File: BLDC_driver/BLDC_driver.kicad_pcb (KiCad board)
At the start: 2 copper layers, 96 parts, among them J1 POWER, J2 CTRL, J3 JTAG, J4 USB-C 16P, Q1 AOTL66912, Q2 AOTL66912, Q3 AOTL66912, Q4 AOTL66912, Q5 AOTL66912, Q6 AOTL66912, SW1 BTN, SW2 BTN, U1 STM32F412CEUx, U2 W25Q128JVS, U3 USBLC6-2SC6, Y1 25MHz

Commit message: Layout progress
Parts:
- added R13: 500u, Marijn_KiCad:CSS2H-3920R-xxxx, F.Cu at (39.1, 111.4)
- added R14: 500u, Marijn_KiCad:CSS2H-3920R-xxxx, F.Cu at (54.1, 111.4)
- added R15: 500u, Marijn_KiCad:CSS2H-3920R-xxxx, F.Cu at (69.1, 111.4)
- J1: footprint TerminalBlock:TerminalBlock_Xinya_XY308-2.54-2P_1x02_P2.54mm_Horizontal -> Connector_AMASS:AMASS_XT60-F_1x02_P7.20mm_Vertical
- moved C10 114.8 mm to (43.6, 145.7), turned to 180 degrees
- moved C13 104.0 mm to (43.6, 115.7), turned to 180 degrees
- moved C11 100.1 mm to (58.6, 145.7), turned to 180 degrees
- moved J1 91.2 mm to (79.7, 98.8), turned to 180 degrees
- moved C14 88.7 mm to (58.6, 115.7), turned to 180 degrees
- moved C12 85.5 mm to (73.6, 145.7), turned to 180 degrees
- moved C15 73.5 mm to (73.6, 115.7), turned to 180 degrees
- moved Q4 45.4 mm to (69.7, 123.8)
- moved Q3 44.3 mm to (69.7, 153.8), turned to -90 degrees
- moved R8 41.4 mm to (95.8, 137.8)
- moved R10 41.4 mm to (95.8, 142.8)
- moved R7 41.4 mm to (95.8, 135.3)
- moved R9 41.4 mm to (95.8, 140.3)
- moved Q2 36.2 mm to (54.7, 153.8), turned to -90 degrees
- moved Q5 34.2 mm to (54.7, 123.8)
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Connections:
- net Net-(Q4-S) renamed /phase_logic/C_CSP
- net Net-(Q5-S) renamed /phase_logic/B_CSP
- net Net-(Q6-S) renamed /phase_logic/A_CSP
- J1 pad 1: +24V -> VPWR

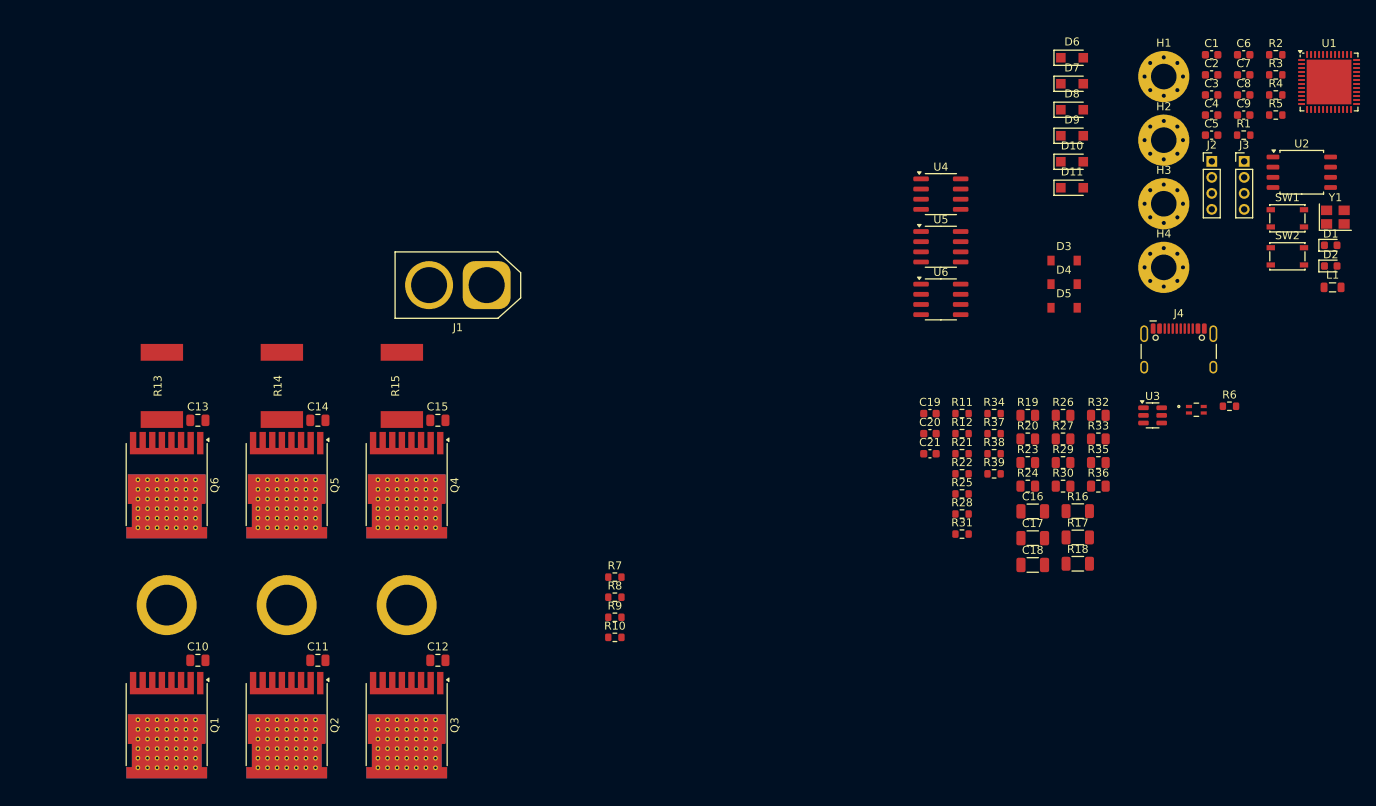
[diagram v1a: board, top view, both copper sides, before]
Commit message: Rough inverter stage layout
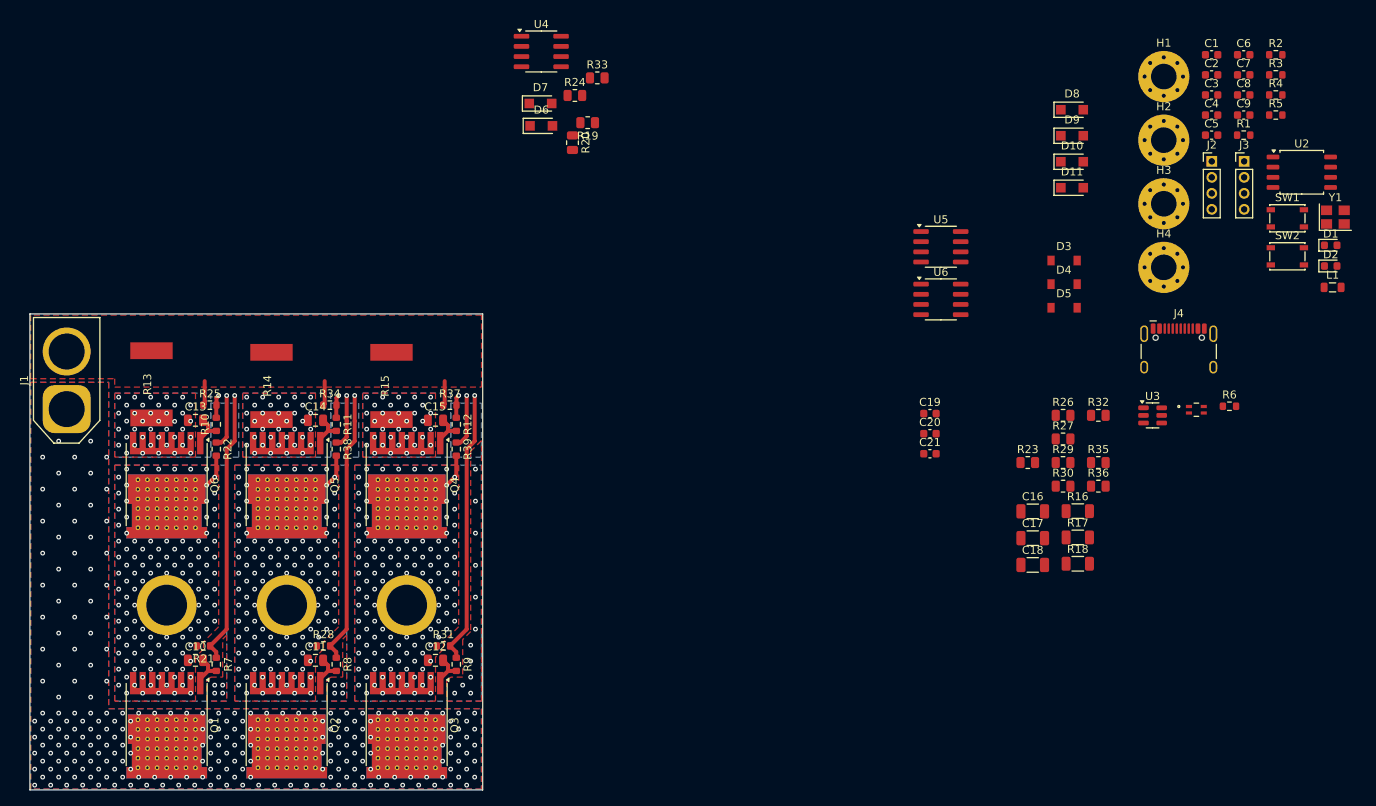
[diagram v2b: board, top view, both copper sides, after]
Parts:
- removed U1: STM32F412CEUx, Package_DFN_QFN:QFN-48-1EP_7x7mm_P0.5mm_EP5.6x5.6mm
- moved R21 97.8 mm to (44.3, 143.9)
- moved R25 94.7 mm to (45.1, 113.8)
- moved R22 93.3 mm to (45.9, 119.3), turned to -90 degrees
- moved R34 83.0 mm to (60.1, 113.8)
- moved R38 82.2 mm to (60.9, 119.3), turned to -90 degrees
- moved R28 81.5 mm to (59.3, 143.9)
- moved R11 78.2 mm to (60.9, 116.2), turned to -90 degrees
- moved R33 77.2 mm to (93.6, 72.9)
- moved R24 74.8 mm to (90.8, 75.1)
- moved R37 68.1 mm to (75.1, 113.8)
- moved R20 67.9 mm to (90.5, 81.0), turned to -90 degrees
- moved R39 67.3 mm to (75.9, 119.3), turned to -90 degrees
- moved D6 66.9 mm to (86.6, 78.9)
- moved D7 66.5 mm to (86.5, 76.1)
- moved R31 66.3 mm to (74.3, 143.9)
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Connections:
- net Net-(Q1-S) renamed /phase_logic/A
- net Net-(Q2-S) renamed /phase_logic/B
- net Net-(Q3-S) renamed /phase_logic/C
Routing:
- net Net-(D9-A): track 0.00 -> 34.4 mm, vias 0 -> 1
- net Net-(D8-A): track 0.00 -> 34.4 mm, vias 0 -> 1
- net Net-(D6-A): track 0.00 -> 34.4 mm, vias 0 -> 1
- net GND: track 0.00 -> 9.52 mm
- net /phase_logic/PHA: track 0.00 -> 6.78 mm, vias 0 -> 1
- net /phase_logic/PHB: track 0.00 -> 6.78 mm, vias 0 -> 1
- net /phase_logic/PHC: track 0.00 -> 6.72 mm, vias 0 -> 1
- net Net-(Q4-G): track 0.00 -> 4.54 mm
- net Net-(Q6-G): track 0.00 -> 4.54 mm
- net Net-(Q5-G): track 0.00 -> 4.54 mm
- net Net-(Q3-G): track 0.00 -> 4.54 mm
- net Net-(Q2-G): track 0.00 -> 4.54 mm
- net Net-(Q1-G): track 0.00 -> 4.54 mm
- net /phase_logic/C: track 0.00 -> 4.17 mm, vias 0 -> 132
- net /phase_logic/B: track 0.00 -> 4.17 mm, vias 0 -> 124
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- added copper zone on B.Cu, net /phase_logic/A
- added copper zone on F.Cu, net /phase_logic/A
- added copper zone on B.Cu, net /phase_logic/A_CSP
- added copper zone on F.Cu, net /phase_logic/A_CSP
- added copper zone on B.Cu, net /phase_logic/B
- added copper zone on F.Cu, net /phase_logic/B
- added copper zone on B.Cu, net /phase_logic/B_CSP
- added copper zone on F.Cu, net /phase_logic/B_CSP
- added copper zone on B.Cu, net /phase_logic/C
- added copper zone on F.Cu, net /phase_logic/C
- added copper zone on B.Cu, net /phase_logic/C_CSP
- added copper zone on F.Cu, net /phase_logic/C_CSP
- added copper zone on F.Cu, net GND
- added copper zone on B.Cu, net VPWR
- added copper zone on F.Cu, net VPWR
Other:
- board outline added: 56.6 x 59.5 mm
- copper layers 2 -> 4

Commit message: Layout progress
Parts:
- moved R23 106.6 mm to (43.0, 99.0)
- moved C16 101.8 mm to (52.0, 93.0), turned to -90 degrees
- moved R32 99.5 mm to (58.0, 99.0)
- moved D10 93.5 mm to (60.9, 100.0), turned to -90 degrees
- moved D8 92.6 mm to (63.2, 100.0), turned to -90 degrees
- moved C21 91.0 mm to (47.1, 96.9), turned to 180 degrees
- moved C17 89.2 mm to (67.0, 93.0), turned to -90 degrees
- moved R27 87.3 mm to (66.1, 101.0), turned to 180 degrees
- moved R26 87.1 mm to (66.1, 99.0), turned to 180 degrees
- moved D11 78.3 mm to (75.7, 99.9), turned to -90 degrees
- moved C19 75.2 mm to (62.1, 96.9), turned to 180 degrees
- moved U5 74.4 mm to (62.1, 93.4), turned to 180 degrees
- moved H2 72.7 mm to (96.1, 55.7)
- moved H1 60.2 mm to (106.5, 56.0)
- moved U6 56.8 mm to (81.2, 87.6)
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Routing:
- net /phase_logic/PHB: track 6.78 -> 32.1 mm, vias 1 -> 2
- net /phase_logic/PHA: track 6.78 -> 31.9 mm, vias 1 -> 2
- net Net-(D10-A): track 2.90 -> 18.6 mm, vias 1 -> 2
- net Net-(D7-A): track 2.90 -> 18.6 mm, vias 1 -> 2
- net Net-(D8-A): track 34.4 -> 50.0 mm, vias 1 -> 2
- net Net-(D6-A): track 34.4 -> 49.9 mm, vias 1 -> 2
- net /phase_logic/HSA: track 0.00 -> 12.0 mm
- net /phase_logic/HSB: track 0.00 -> 12.0 mm
- net GND: track 9.52 -> 17.9 mm
- net /phase_logic/LSB: track 0.00 -> 7.56 mm
- net /phase_logic/LSA: track 0.00 -> 7.50 mm
- net +12V: track 0.00 -> 5.81 mm
- net Net-(U4-HB): track 0.00 -> 2.66 mm
- net Net-(U5-HB): track 0.00 -> 2.66 mm
- net Net-(D8-K): track 0.00 -> 2.15 mm
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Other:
- board size 56.6 x 59.5 mm -> 75 x 85 mm
- board text added: "TODO: Bypass CAPS"
- board text added: "TODO: define inverter / power area"
- board text added: "TODO: middle layers in inverter stage"
- board text added: "TODO: stitching"

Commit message: Update
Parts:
- moved D9 60.0 mm to (78.2, 100.0), turned to -90 degrees
- moved R35 53.6 mm to (73.0, 99.0)
- moved R36 53.6 mm to (73.0, 101.0)
- moved R29 41.1 mm to (81.1, 99.0), turned to 180 degrees
- moved R30 41.1 mm to (81.1, 101.0), turned to 180 degrees
- moved C18 40.3 mm to (82.0, 93.0), turned to -90 degrees
- moved C20 30.4 mm to (77.1, 96.9), turned to 180 degrees
- moved U6 7.10 mm to (77.1, 93.4), turned to 180 degrees
- moved D11 0.29 mm to (75.9, 100.0)
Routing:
- net /phase_logic/PHC: track 6.72 -> 32.1 mm, vias 1 -> 2
- net Net-(D11-A): track 2.90 -> 18.5 mm, vias 1 -> 2
- net Net-(D9-A): track 34.4 -> 49.8 mm, vias 1 -> 2
- net /phase_logic/HSC: track 0.00 -> 12.0 mm
- net /phase_logic/LSC: track 0.00 -> 7.53 mm
- net GND: track 17.9 -> 22.0 mm
- net +12V: track 5.81 -> 8.68 mm
- net Net-(U6-HB): track 0.00 -> 2.66 mm
- net Net-(D11-K): track 0.00 -> 2.15 mm
- net Net-(D9-K): track 0.00 -> 2.15 mm

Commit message: New design
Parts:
- added C22: 3.3nF, Capacitor_SMD:C_0805_2012Metric, F.Cu at (209.6, 65.7)
- added C23: 3.3nF, Capacitor_SMD:C_0805_2012Metric, F.Cu at (288.3, 42.0)
- added C24: 3.3nF, Capacitor_SMD:C_0805_2012Metric, F.Cu at (288.3, 45.0)
- added C25: 3.3nF, Capacitor_SMD:C_0805_2012Metric, F.Cu at (209.6, 49.1)
- added C26: 3.3nF, Capacitor_SMD:C_0805_2012Metric, F.Cu at (238.4, 122.6)
- added C27: 3.3nF, Capacitor_SMD:C_0805_2012Metric, F.Cu at (238.4, 125.6)
- added C28: 3.3nF, Capacitor_SMD:C_0805_2012Metric, F.Cu at (209.6, 32.4)
- added C29: 3.3nF, Capacitor_SMD:C_0805_2012Metric, F.Cu at (259.7, 122.6)
- added C30: 3.3nF, Capacitor_SMD:C_0805_2012Metric, F.Cu at (259.7, 125.6)
- added C31: 3.3nF, Capacitor_SMD:C_0805_2012Metric, F.Cu at (192.7, 49.1)
- added C32: 3.3nF, Capacitor_SMD:C_0805_2012Metric, F.Cu at (217.1, 122.6)
- added C33: 3.3nF, Capacitor_SMD:C_0805_2012Metric, F.Cu at (217.1, 125.6)
- added C34: 3.3nF, Capacitor_SMD:C_0805_2012Metric, F.Cu at (192.7, 32.4)
- added C35: 3.3nF, Capacitor_SMD:C_0805_2012Metric, F.Cu at (281.0, 122.6)
- added C36: 3.3nF, Capacitor_SMD:C_0805_2012Metric, F.Cu at (281.0, 125.6)
- added C37: 3.3nF, Capacitor_SMD:C_0805_2012Metric, F.Cu at (192.7, 65.7)
- added HS1: SK_92/50_SA, Marijn_KiCad:SK_92-50_SA, B.Cu at (112.0, 112.0)
- added Q10: AOTL66912, Package_TO_SOT_SMD:Infineon_PG-HSOF-8-1_ThermalVias, F.Cu at (130.0, 101.3)
- added Q11: AOTL66912, Package_TO_SOT_SMD:Infineon_PG-HSOF-8-1_ThermalVias, F.Cu at (130.0, 112.0)
- added Q12: AOTL66912, Package_TO_SOT_SMD:Infineon_PG-HSOF-8-1_ThermalVias, F.Cu at (130.0, 122.7)
- added Q13: AOTL66912, Package_TO_SOT_SMD:Infineon_PG-HSOF-8-1_ThermalVias, F.Cu at (94.0, 134.6)
- added Q14: AOTL66912, Package_TO_SOT_SMD:Infineon_PG-HSOF-8-1_ThermalVias, F.Cu at (94.0, 145.3)
- added Q15: AOTL66912, Package_TO_SOT_SMD:Infineon_PG-HSOF-8-1_ThermalVias, F.Cu at (94.0, 156.0)
- added Q16: AOTL66912, Package_TO_SOT_SMD:Infineon_PG-HSOF-8-1_ThermalVias, F.Cu at (130.0, 134.6)
- added Q17: AOTL66912, Package_TO_SOT_SMD:Infineon_PG-HSOF-8-1_ThermalVias, F.Cu at (130.0, 145.3)
- added Q18: AOTL66912, Package_TO_SOT_SMD:Infineon_PG-HSOF-8-1_ThermalVias, F.Cu at (130.0, 156.0)
- added Q7: AOTL66912, Package_TO_SOT_SMD:Infineon_PG-HSOF-8-1_ThermalVias, F.Cu at (94.0, 101.3)
- added Q8: AOTL66912, Package_TO_SOT_SMD:Infineon_PG-HSOF-8-1_ThermalVias, F.Cu at (94.0, 112.0)
- added Q9: AOTL66912, Package_TO_SOT_SMD:Infineon_PG-HSOF-8-1_ThermalVias, F.Cu at (94.0, 122.7)
- added R40: 2R2, Resistor_SMD:R_0603_1608Metric, F.Cu at (238.2, 128.3)
- added R41: 2R2, Resistor_SMD:R_0603_1608Metric, F.Cu at (238.2, 130.9)
- added R42: 2R2, Resistor_SMD:R_0603_1608Metric, F.Cu at (213.8, 32.1)
- added R43: 2R2, Resistor_SMD:R_0603_1608Metric, F.Cu at (259.5, 128.3)
- added R44: 2R2, Resistor_SMD:R_0603_1608Metric, F.Cu at (259.5, 130.9)
- added R45: 2R2, Resistor_SMD:R_0603_1608Metric, F.Cu at (196.9, 48.8)
- added R46: 2R2, Resistor_SMD:R_0603_1608Metric, F.Cu at (216.9, 128.3)
- added R47: 2R2, Resistor_SMD:R_0603_1608Metric, F.Cu at (216.9, 130.9)
- added R48: 2R2, Resistor_SMD:R_0603_1608Metric, F.Cu at (196.9, 32.1)
- added R49: 2R2, Resistor_SMD:R_0603_1608Metric, F.Cu at (280.8, 128.3)
- added R50: 2R2, Resistor_SMD:R_0603_1608Metric, F.Cu at (280.8, 130.9)
- added R51: 2R2, Resistor_SMD:R_0603_1608Metric, F.Cu at (196.9, 65.5)
- added U1: STM32F412CEUx, Package_DFN_QFN:QFN-48-1EP_7x7mm_P0.5mm_EP5.6x5.6mm, F.Cu at (187.6, 136.2)
- C1, C2, C3, C4: value 100n -> 820u/100v; footprint Capacitor_SMD:C_0603_1608Metric -> Capacitor_THT:C_Radial_D18.0mm_H35.5mm_P7.50mm; moved to B.Cu
- C10, C11, C14: value 3.3nF -> 100n; footprint Capacitor_SMD:C_0805_2012Metric -> Capacitor_SMD:C_0603_1608Metric
- C12, C13: value 3.3nF -> 12p; footprint Capacitor_SMD:C_0805_2012Metric -> Capacitor_SMD:C_0603_1608Metric
- C15: value 3.3nF -> 4u7/25V; footprint Capacitor_SMD:C_0805_2012Metric -> Capacitor_SMD:C_1206_3216Metric
- C16, C18: value 4u7/25V -> 100n; footprint Capacitor_SMD:C_1206_3216Metric -> Capacitor_SMD:C_0603_1608Metric
- C19: value 100n -> 4u7/25V; footprint Capacitor_SMD:C_0603_1608Metric -> Capacitor_SMD:C_1206_3216Metric
- C20, C21: value 100n -> 3.3nF; footprint Capacitor_SMD:C_0603_1608Metric -> Capacitor_SMD:C_0805_2012Metric
- C5: value 4u7 -> 100n
- C8: value 12p -> 100n
- C9: value 12p -> 4u7
- D10, D11, D9: value PMEG6010ER,115 -> SL110PL; footprint Diode_SMD:Nexperia_CFP3_SOD-123W -> Marijn_KiCad:SOD-123FL
- D3, D4, D5: value SL110PL -> PMEG6010ER,115; footprint Marijn_KiCad:SOD-123FL -> Diode_SMD:Nexperia_CFP3_SOD-123W
- J1: value POWER -> CTRL; footprint Connector_AMASS:AMASS_XT60-F_1x02_P7.20mm_Vertical -> Connector_PinHeader_2.00mm:PinHeader_1x04_P2.00mm_Vertical
- J2: value CTRL -> POWER; footprint Connector_PinHeader_2.00mm:PinHeader_1x04_P2.00mm_Vertical -> Connector_AMASS:AMASS_XT60-F_1x02_P7.20mm_Vertical
- R10, R11, R12, R22, R7, R8, R9: value 2R2 -> 10R; footprint Resistor_SMD:R_0603_1608Metric -> Resistor_SMD:R_0805_2012Metric
- R13, R14, R15: value 500u -> 47R; footprint Marijn_KiCad:CSS2H-3920R-xxxx -> Resistor_SMD:R_0603_1608Metric
- R16, R17, R18: value 33k -> 2R2; footprint Resistor_SMD:R_1206_3216Metric -> Resistor_SMD:R_0603_1608Metric
- R21: value 47R -> 10R; footprint Resistor_SMD:R_0603_1608Metric -> Resistor_SMD:R_0805_2012Metric
- R25: value 47R -> 200u; footprint Resistor_SMD:R_0603_1608Metric -> Marijn_KiCad:CSS2H-3920R-xxxx
- R26, R27: value 10R -> 200u; footprint Resistor_SMD:R_0805_2012Metric -> Marijn_KiCad:CSS2H-3920R-xxxx
- R29, R30: value 10R -> 47R; footprint Resistor_SMD:R_0805_2012Metric -> Resistor_SMD:R_0603_1608Metric
- R31: value 47R -> 33k; footprint Resistor_SMD:R_0603_1608Metric -> Resistor_SMD:R_1206_3216Metric
- R32, R33: value 10R -> 33k; footprint Resistor_SMD:R_0805_2012Metric -> Resistor_SMD:R_1206_3216Metric
- R34, R37: value 47R -> 2R2
- R35, R36: value 10R -> 2R2; footprint Resistor_SMD:R_0805_2012Metric -> Resistor_SMD:R_0603_1608Metric
- moved C21 242.7 mm to (288.3, 70.3), turned to 0 degrees
- moved R38 237.4 mm to (288.1, 50.2), turned to 0 degrees
- moved R34 231.6 mm to (288.1, 73.1)
- moved R37 223.0 mm to (288.1, 47.7)
- moved R35 216.3 mm to (288.1, 75.6)
- moved C20 213.3 mm to (288.3, 67.3), turned to 0 degrees
- moved R21 176.6 mm to (213.4, 93.0)
- moved R24 170.4 mm to (213.4, 101.8)
- moved R23 170.4 mm to (213.4, 98.9)
- moved R22 169.1 mm to (213.4, 95.9), turned to 0 degrees
- moved R7 167.4 mm to (204.6, 93.0), turned to 0 degrees
- moved R13 166.6 mm to (204.4, 112.1), turned to 0 degrees
- moved J1 163.1 mm to (190.2, 121.0), turned to 0 degrees
- moved D10 163.1 mm to (224.0, 95.9), turned to 0 degrees
- moved R33 160.6 mm to (218.4, 109.8)
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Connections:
- net /phase_logic/A_HI renamed /inverter stage/A_HI
- net /phase_logic/A_LI renamed /inverter stage/A_LI
- net /phase_logic/B_HI renamed /inverter stage/B_HI
- net /phase_logic/B_LI renamed /inverter stage/B_LI
- net /phase_logic/C_HI renamed /inverter stage/C_HI
- net /phase_logic/C_LI renamed /inverter stage/C_LI
- C1 pad 1: +3V3 -> VPWR
- C10 pad 1: Net-(Q1-G) -> +3.3VA
- C10 pad 2: /phase_logic/A -> GND
- C11 pad 1: Net-(Q2-G) -> GND
- C11 pad 2: /phase_logic/B -> /NRST
- C12 pad 1: Net-(Q3-G) -> /HSE_IN
- C12 pad 2: /phase_logic/C -> GND
- C13 pad 1: Net-(Q6-G) -> Net-(C13-Pad1)
- C13 pad 2: /phase_logic/A_CSP -> GND
- C14 pad 1: Net-(Q5-G) -> +12V
- C14 pad 2: /phase_logic/B_CSP -> GND
- C15 pad 1: Net-(Q4-G) -> /inverter stage/PHA
- C15 pad 2: /phase_logic/C_CSP -> Net-(U4-HB)
- C16 pad 1: /phase_logic/PHA -> +12V
- C16 pad 2: Net-(U4-HB) -> GND
- C17 pad 1: /phase_logic/PHB -> /inverter stage/PHB
- C18 pad 1: /phase_logic/PHC -> +12V
- C18 pad 2: Net-(U6-HB) -> GND
- C19 pad 1: +12V -> /inverter stage/PHC
- C19 pad 2: GND -> Net-(U6-HB)
- C2 pad 1: +3V3 -> VPWR
- C20 pad 1: +12V -> Net-(Q1-G)
- C20 pad 2: GND -> /inverter stage/A
- C21 pad 1: +12V -> Net-(Q2-G)
- C21 pad 2: GND -> /inverter stage/A
- C3 pad 1: +3V3 -> VPWR
- C4 pad 1: +3V3 -> VPWR
- C6 pad 1: +3.3VA -> +3V3
- C7 pad 1: GND -> +3V3
- C7 pad 2: /NRST -> GND
- C8 pad 1: /HSE_IN -> +3V3
- C9 pad 1: Net-(C9-Pad1) -> +3V3
- D10 pad 1: Net-(D10-K) -> /inverter stage/PHB
- D10 pad 2: Net-(D10-A) -> GND
- D11 pad 1: Net-(D11-K) -> /inverter stage/PHC
- D11 pad 2: Net-(D11-A) -> GND
- D3 pad 1: /phase_logic/PHA -> Net-(D3-K)
- D3 pad 2: GND -> /inverter stage/HA
- D4 pad 1: /phase_logic/PHB -> Net-(D4-K)
- D4 pad 2: GND -> /inverter stage/HB
- D5 pad 1: /phase_logic/PHC -> Net-(D5-K)
- D5 pad 2: GND -> /inverter stage/HC
- D6 pad 2: Net-(D6-A) -> /inverter stage/LA
- D7 pad 2: Net-(D7-A) -> /inverter stage/LB
- D8 pad 2: Net-(D8-A) -> /inverter stage/LC
- D9 pad 1: Net-(D9-K) -> /inverter stage/PHA
- D9 pad 2: Net-(D9-A) -> GND
- J1 pad 1: VPWR -> /CTRL_SPI_MOSI
- J1 pad 2: GND -> /CTRL_SPI_MISO
- J2 pad 1: /CTRL_SPI_MOSI -> VPWR
- J2 pad 2: /CTRL_SPI_MISO -> GND
- J5 pad 1: /phase_logic/A -> /inverter stage/A
- J6 pad 1: /phase_logic/B -> /inverter stage/B
- J7 pad 1: /phase_logic/C -> /inverter stage/C
- Q1 pad 2: /phase_logic/A -> /inverter stage/A
- Q2 pad 2: /phase_logic/B -> /inverter stage/A
- Q3 pad 2: /phase_logic/C -> /inverter stage/A
- Q4 pad 2: /phase_logic/C_CSP -> /inverter stage/A_CSP
- Q4 pad 3: /phase_logic/C -> /inverter stage/A
- Q5 pad 2: /phase_logic/B_CSP -> /inverter stage/A_CSP
- Q5 pad 3: /phase_logic/B -> /inverter stage/A
- Q6 pad 2: /phase_logic/A_CSP -> /inverter stage/A_CSP
- Q6 pad 3: /phase_logic/A -> /inverter stage/A
- R10 pad 1: Net-(D7-A) -> /inverter stage/HSA
- R10 pad 2: Net-(Q6-G) -> /inverter stage/HA
- R11 pad 1: Net-(D10-A) -> /inverter stage/HSB
- R11 pad 2: Net-(Q5-G) -> /inverter stage/HB
- R12 pad 1: Net-(D11-A) -> /inverter stage/HSC
- R12 pad 2: Net-(Q4-G) -> /inverter stage/HC
- R13 pad 1: /phase_logic/A_CSP -> /inverter stage/A
- R13 pad 2: GND -> /inverter stage/HA
- R14 pad 1: /phase_logic/B_CSP -> /inverter stage/B
- R14 pad 2: GND -> /inverter stage/HB
- R15 pad 1: /phase_logic/C_CSP -> /inverter stage/C
- R15 pad 2: GND -> /inverter stage/HC
- R16 pad 1: GND -> /inverter stage/PHA
- R16 pad 2: /phase_logic/PHA -> /inverter stage/A
- R17 pad 1: GND -> /inverter stage/PHB
- R17 pad 2: /phase_logic/PHB -> /inverter stage/B
- R18 pad 1: GND -> /inverter stage/PHC
- R18 pad 2: /phase_logic/PHC -> /inverter stage/C
- R19 pad 1: /phase_logic/HSA -> /inverter stage/LSA
- R20 pad 1: /phase_logic/HSA -> /inverter stage/LSB
- R20 pad 2: Net-(D6-A) -> Net-(D7-K)
- R21 pad 1: /phase_logic/A -> /inverter stage/LSC
- R21 pad 2: Net-(D6-A) -> Net-(D8-K)
- R22 pad 1: /phase_logic/PHA -> /inverter stage/LSA
- R22 pad 2: /phase_logic/A -> /inverter stage/LA
- R23 pad 1: /phase_logic/LSA -> /inverter stage/LSB
- R23 pad 2: Net-(D7-K) -> /inverter stage/LB
- R24 pad 1: /phase_logic/LSA -> /inverter stage/LSC
- R24 pad 2: Net-(D7-A) -> /inverter stage/LC
- R25 pad 1: GND -> /inverter stage/A_CSP
- R25 pad 2: Net-(D7-A) -> GND
- R26 pad 1: /phase_logic/HSB -> /inverter stage/B_CSP
- R26 pad 2: Net-(D8-K) -> GND
- R27 pad 1: /phase_logic/HSB -> /inverter stage/C_CSP
- R27 pad 2: Net-(D8-A) -> GND
- R28 pad 1: /phase_logic/B -> GND
- R28 pad 2: Net-(D8-A) -> /inverter stage/LA
- R29 pad 1: /phase_logic/HSC -> GND
- R29 pad 2: Net-(D9-K) -> /inverter stage/LB
- R30 pad 1: /phase_logic/HSC -> GND
- R30 pad 2: Net-(D9-A) -> /inverter stage/LC
- R31 pad 1: /phase_logic/C -> GND
- R31 pad 2: Net-(D9-A) -> /inverter stage/PHA
- R32 pad 1: /phase_logic/LSB -> GND
- R32 pad 2: Net-(D10-K) -> /inverter stage/PHB
- R33 pad 1: /phase_logic/LSB -> GND
- R33 pad 2: Net-(D10-A) -> /inverter stage/PHC
- R34 pad 1: GND -> /inverter stage/HA
- R34 pad 2: Net-(D10-A) -> Net-(Q1-G)
- R35 pad 1: /phase_logic/LSC -> /inverter stage/HA
- R35 pad 2: Net-(D11-K) -> Net-(Q2-G)
- R36 pad 1: /phase_logic/LSC -> /inverter stage/HA
- R36 pad 2: Net-(D11-A) -> Net-(Q3-G)
- R37 pad 1: GND -> /inverter stage/LA
- R37 pad 2: Net-(D11-A) -> Net-(Q4-G)
- R38 pad 1: /phase_logic/PHB -> /inverter stage/LA
- R38 pad 2: /phase_logic/B -> Net-(Q5-G)
- R39 pad 1: /phase_logic/PHC -> /inverter stage/LA
- R39 pad 2: /phase_logic/C -> Net-(Q6-G)
- R4 pad 2: Net-(C9-Pad1) -> Net-(C13-Pad1)
- R7 pad 1: Net-(D6-A) -> /inverter stage/HSA
- R7 pad 2: Net-(Q1-G) -> Net-(D3-K)
- R8 pad 1: Net-(D8-A) -> /inverter stage/HSB
- R8 pad 2: Net-(Q2-G) -> Net-(D4-K)
- R9 pad 1: Net-(D9-A) -> /inverter stage/HSC
- R9 pad 2: Net-(Q3-G) -> Net-(D5-K)
- U4 pad 3: /phase_logic/HSA -> /inverter stage/HSA
- U4 pad 4: /phase_logic/PHA -> /inverter stage/PHA
- U4 pad 8: /phase_logic/LSA -> /inverter stage/LSA
- U5 pad 3: /phase_logic/HSB -> /inverter stage/HSB
- U5 pad 4: /phase_logic/PHB -> /inverter stage/PHB
- U5 pad 8: /phase_logic/LSB -> /inverter stage/LSB
- U6 pad 3: /phase_logic/HSC -> /inverter stage/HSC
- U6 pad 4: /phase_logic/PHC -> /inverter stage/PHC
- U6 pad 8: /phase_logic/LSC -> /inverter stage/LSC
- Y1 pad 3: Net-(C9-Pad1) -> Net-(C13-Pad1)
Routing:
- net Net-(D8-A): track 50.0 -> 0.00 mm, vias 2 -> 0
- net Net-(D6-A): track 49.9 -> 0.00 mm, vias 2 -> 0
- net Net-(D9-A): track 49.8 -> 0.00 mm, vias 2 -> 0
- net /phase_logic/PHB: track 32.1 -> 0.00 mm, vias 2 -> 0
- net /phase_logic/PHC: track 32.1 -> 0.00 mm, vias 2 -> 0
- net /phase_logic/PHA: track 31.9 -> 0.00 mm, vias 2 -> 0
- net GND: track 22.0 -> 0.00 mm
- net Net-(D10-A): track 18.6 -> 0.00 mm, vias 2 -> 0
- net Net-(D7-A): track 18.6 -> 0.00 mm, vias 2 -> 0
- net Net-(D11-A): track 18.5 -> 0.00 mm, vias 2 -> 0
- net /phase_logic/HSA: track 12.0 -> 0.00 mm
- net /phase_logic/HSC: track 12.0 -> 0.00 mm
- net /phase_logic/HSB: track 12.0 -> 0.00 mm
- net +12V: track 8.68 -> 0.00 mm
- net /phase_logic/LSB: track 7.56 -> 0.00 mm
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- added copper zone on B.Cu, net /inverter stage/A
- added copper zone on F.Cu, net /inverter stage/A
- added copper zone on B.Cu, net /inverter stage/A_CSP
- added copper zone on F.Cu, net /inverter stage/A_CSP
- added copper zone on B.Cu, net /inverter stage/B
- added copper zone on F.Cu, net /inverter stage/B
- added copper zone on B.Cu, net /inverter stage/B_CSP
- added copper zone on F.Cu, net /inverter stage/B_CSP
- added copper zone on B.Cu, net /inverter stage/C
- added copper zone on F.Cu, net /inverter stage/C
- added copper zone on B.Cu, net /inverter stage/C_CSP
- added copper zone on F.Cu, net /inverter stage/C_CSP
- added copper zone on B.Cu, net GND
- added copper zone on In1.Cu, net GND
- added copper zone on In2.Cu, net GND
- added copper zone on In1.Cu, net VPWR
- removed copper zone on B.Cu, net /phase_logic/A
- removed copper zone on F.Cu, net /phase_logic/A
- removed copper zone on B.Cu, net /phase_logic/A_CSP
- removed copper zone on F.Cu, net /phase_logic/A_CSP
- removed copper zone on B.Cu, net /phase_logic/B
- removed copper zone on F.Cu, net /phase_logic/B
- removed copper zone on B.Cu, net /phase_logic/B_CSP
- removed copper zone on F.Cu, net /phase_logic/B_CSP
- removed copper zone on B.Cu, net /phase_logic/C
- removed copper zone on F.Cu, net /phase_logic/C
- removed copper zone on B.Cu, net /phase_logic/C_CSP
- removed copper zone on F.Cu, net /phase_logic/C_CSP
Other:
- board size 75 x 85 mm -> 100 x 100 mm
- board text removed: "TODO: Bypass CAPS"
- board text removed: "TODO: define inverter / power area"
- board text removed: "TODO: middle layers in inverter stage"
- board text removed: "TODO: stitching"

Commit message: Layout progress
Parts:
- removed the R34 at (288.1, 73.1)
- removed the R35 at (288.1, 75.6)
- removed the R36 at (213.8, 65.5)
- removed R37, R38, R39, R40, R41, R42, R43, R44, R45, R46, R47, R48, R49, R50, R51: 2R2, Resistor_SMD:R_0603_1608Metric
- added R26: 500u, Marijn_KiCad:CSS2H-3920R-xxxx, F.Cu at (142.9, 68.0)
- added R28: 500u, Marijn_KiCad:CSS2H-3920R-xxxx, F.Cu at (142.9, 122.7)
- added R30: 500u, Marijn_KiCad:CSS2H-3920R-xxxx, F.Cu at (142.9, 156.0)
- R25: value 200u -> 500u
- R27: renamed from R26; value 200u -> 500u
- R29: renamed from R27; value 200u -> 500u
- moved C21 186.1 mm to (102.7, 82.9)
- moved C20 185.7 mm to (102.7, 72.2)
- moved C34 156.4 mm to (102.7, 160.2)
- moved C24 153.4 mm to (139.7, 82.9), turned to 180 degrees
- moved C23 151.6 mm to (139.7, 72.2), turned to 180 degrees
- moved C36 143.3 mm to (139.7, 149.5), turned to 180 degrees
- moved C28 142.7 mm to (102.7, 126.9)
- moved C35 142.2 mm to (139.7, 138.8), turned to 180 degrees
- moved C26 136.8 mm to (102.7, 105.5)
- moved C27 136.0 mm to (102.7, 116.2)
- moved C29 121.2 mm to (139.7, 105.5), turned to 180 degrees
- moved C30 120.3 mm to (139.7, 116.2), turned to 180 degrees
- moved C33 116.9 mm to (102.7, 149.5)
- moved C32 115.6 mm to (102.7, 138.8)
- moved C22 110.4 mm to (102.7, 93.6)
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- renumbered R28 to R31, R29 to R32, R30 to R33, R31 to R34, R32 to R35, R33 to R36
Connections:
- C20 pad 1: Net-(Q1-G) -> /inverter stage/HA
- C21 pad 1: Net-(Q2-G) -> /inverter stage/HA
- C22 pad 1: Net-(Q3-G) -> /inverter stage/HA
- C23 pad 1: Net-(Q4-G) -> /inverter stage/LA
- C24 pad 1: Net-(Q5-G) -> /inverter stage/LA
- C25 pad 1: Net-(Q6-G) -> /inverter stage/LA
- C26 pad 1: Net-(Q7-G) -> /inverter stage/HB
- C27 pad 1: Net-(Q8-G) -> /inverter stage/HB
- C28 pad 1: Net-(Q9-G) -> /inverter stage/HB
- C29 pad 1: Net-(Q10-G) -> /inverter stage/LB
- C30 pad 1: Net-(Q11-G) -> /inverter stage/LB
- C31 pad 1: Net-(Q12-G) -> /inverter stage/LB
- C32 pad 1: Net-(Q13-G) -> /inverter stage/HC
- C33 pad 1: Net-(Q14-G) -> /inverter stage/HC
- C34 pad 1: Net-(Q15-G) -> /inverter stage/HC
- C35 pad 1: Net-(Q16-G) -> /inverter stage/LC
- C36 pad 1: Net-(Q17-G) -> /inverter stage/LC
- C37 pad 1: Net-(Q18-G) -> /inverter stage/LC
- Q1 pad 1: Net-(Q1-G) -> /inverter stage/HA
- Q10 pad 1: Net-(Q10-G) -> /inverter stage/LB
- Q11 pad 1: Net-(Q11-G) -> /inverter stage/LB
- Q12 pad 1: Net-(Q12-G) -> /inverter stage/LB
- Q13 pad 1: Net-(Q13-G) -> /inverter stage/HC
- Q14 pad 1: Net-(Q14-G) -> /inverter stage/HC
- Q15 pad 1: Net-(Q15-G) -> /inverter stage/HC
- Q16 pad 1: Net-(Q16-G) -> /inverter stage/LC
- Q17 pad 1: Net-(Q17-G) -> /inverter stage/LC
- Q18 pad 1: Net-(Q18-G) -> /inverter stage/LC
- Q2 pad 1: Net-(Q2-G) -> /inverter stage/HA
- Q3 pad 1: Net-(Q3-G) -> /inverter stage/HA
- Q4 pad 1: Net-(Q4-G) -> /inverter stage/LA
- Q5 pad 1: Net-(Q5-G) -> /inverter stage/LA
- Q6 pad 1: Net-(Q6-G) -> /inverter stage/LA
- Q7 pad 1: Net-(Q7-G) -> /inverter stage/HB
- Q8 pad 1: Net-(Q8-G) -> /inverter stage/HB
- Q9 pad 1: Net-(Q9-G) -> /inverter stage/HB
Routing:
- net /inverter stage/HC: track 0.00 -> 104.8 mm
- net /inverter stage/HA: track 0.00 -> 98.6 mm
- net /inverter stage/HB: track 0.00 -> 89.0 mm, vias 0 -> 2
- net /inverter stage/LB: track 0.00 -> 43.6 mm, vias 0 -> 6
- net /inverter stage/LC: track 0.00 -> 43.5 mm, vias 0 -> 6
- net /inverter stage/LA: track 0.00 -> 42.6 mm, vias 0 -> 6
- net /inverter stage/B: track 0.00 -> 23.7 mm, vias 0 -> 2
- net /inverter stage/PHB: track 0.00 -> 11.1 mm
- net Net-(U5-HB): track 0.00 -> 2.69 mm
- net GND: track 0.00 -> 2.22 mm
- net /inverter stage/HSA: track 0.00 -> 2.11 mm
- net /inverter stage/LSC: track 0.00 -> 2.11 mm
- net /inverter stage/HSB: track 0.00 -> 2.11 mm
- net /inverter stage/HSC: track 0.00 -> 2.09 mm
- net /inverter stage/LSB: track 0.00 -> 2.09 mm
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
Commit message: Layout progress
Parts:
- C17, C19, D10, D11, D4, D5, D7, D8, R17, R18, R35, R36: moved to B.Cu
- moved C5 74.8 mm to (250.2, 100.2)
- moved C6 74.8 mm to (250.2, 102.8)
- moved C7 74.8 mm to (250.2, 105.3)
- moved C8 74.8 mm to (250.2, 107.8)
- moved H1 74.8 mm to (244.1, 102.1)
- moved H3 74.8 mm to (244.2, 118.9)
- moved H4 74.8 mm to (244.2, 126.8)
- moved J4 74.8 mm to (277.5, 112.5)
- moved L1 74.8 mm to (250.5, 126.9)
- moved R2 74.8 mm to (258.2, 100.2)
- moved R3 74.8 mm to (258.2, 102.8)
- moved R4 74.8 mm to (258.2, 105.3)
- moved R5 74.8 mm to (258.2, 107.8)
- moved Y1 74.8 mm to (250.8, 123.3)
- moved C9 74.8 mm to (250.2, 110.3)
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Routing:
- net /inverter stage/A: track 1.55 -> 18.0 mm, vias 0 -> 2
- net /inverter stage/HA: track 98.6 -> 85.1 mm
- net /inverter stage/B: track 23.7 -> 10.8 mm
- net /inverter stage/HB: track 89.0 -> 76.6 mm
- net /inverter stage/PHB: track 11.1 -> 0.00 mm
- net /inverter stage/C: track 0.00 -> 11.1 mm, vias 0 -> 2
- net /inverter stage/PHC: track 0.00 -> 6.88 mm, vias 0 -> 1
- net /inverter stage/LA: track 42.6 -> 37.7 mm
- net /inverter stage/LC: track 43.5 -> 39.0 mm, vias 6 -> 7
- net GND: track 2.22 -> 6.39 mm
- net /inverter stage/LB: track 43.6 -> 40.6 mm, vias 6 -> 7
- net Net-(U5-HB): track 2.69 -> 0.00 mm
- net /inverter stage/HSC: track 2.09 -> 4.58 mm
- net /inverter stage/HSA: track 2.11 -> 0.00 mm
- net /inverter stage/LSA: track 2.09 -> 0.00 mm
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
